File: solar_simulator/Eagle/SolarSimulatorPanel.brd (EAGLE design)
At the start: 150 x 70 mm, 82 parts, among them U1 Blue Driver, U2 Red Driver, U3 Green Driver, X1 MKDSN1,5/2-5,08

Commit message: added manufacturer informaton for temp sensors on solar sim, tweaks to 1u_panel, added very in progress driver for solar simulator.  Documentation inboud
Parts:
- R2, R3, R6: value 137 m -> 250 m
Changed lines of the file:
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@@
 <?xml version="1.0" encoding="utf-8"?>
 <!DOCTYPE eagle SYSTEM "eagle.dtd">
-<eagle version="9.3.0">
+<eagle version="9.4.0">
 <drawing>
 <settings>
@@
 <attribute name="VALUE" x="8.725" y="26.6" size="1.016" layer="27" rot="R270"/>
 </element>
-<element name="R6" library="rcl" library_urn="urn:adsk.eagle:library:334" package="R2010" package3d_urn="urn:adsk.eagle:package:23551/2" value="137 m" x="22.8" y="64.9" smashed="yes">
+<element name="R6" library="rcl" library_urn="urn:adsk.eagle:library:334" package="R2010" package3d_urn="urn:adsk.eagle:package:23551/2" value="250 m" x="22.8" y="64.9" smashed="yes">
 <attribute name="NAME" x="22.025" y="67.005" size="0.7" layer="25" font="vector" ratio="20"/>
 <attribute name="SPICEPREFIX" value="R" x="22.8" y="64.9" size="1.778" layer="27" display="off"/>
 <attribute name="VALUE" x="19.625" y="61.725" size="1.27" layer="27"/>
 </element>
-<element name="R2" library="rcl" library_urn="urn:adsk.eagle:library:334" package="R2010" package3d_urn="urn:adsk.eagle:package:23551/2" value="137 m" x="22.7" y="48.9" smashed="yes">
+<element name="R2" library="rcl" library_urn="urn:adsk.eagle:library:334" package="R2010" package3d_urn="urn:adsk.eagle:package:23551/2" value="250 m" x="22.7" y="48.9" smashed="yes">
 <attribute name="NAME" x="22.225" y="50.605" size="0.7" layer="25" font="vector" ratio="20"/>
 <attribute name="SPICEPREFIX" value="R" x="22.7" y="48.9" size="1.778" layer="27" display="off"/>
 <attribute name="VALUE" x="19.525" y="45.725" size="1.27" layer="27"/>
 </element>
-<element name="R3" library="rcl" library_urn="urn:adsk.eagle:library:334" package="R2010" package3d_urn="urn:adsk.eagle:package:23551/2" value="137 m" x="22.7" y="33.2" smashed="yes">
+<element name="R3" library="rcl" library_urn="urn:adsk.eagle:library:334" package="R2010" package3d_urn="urn:adsk.eagle:package:23551/2" value="250 m" x="22.7" y="33.2" smashed="yes">
 <attribute name="NAME" x="22.325" y="35.005" size="0.7" layer="25" font="vector" ratio="20"/>
 <attribute name="SPICEPREFIX" value="R" x="22.7" y="33.2" size="1.778" layer="27" display="off"/>

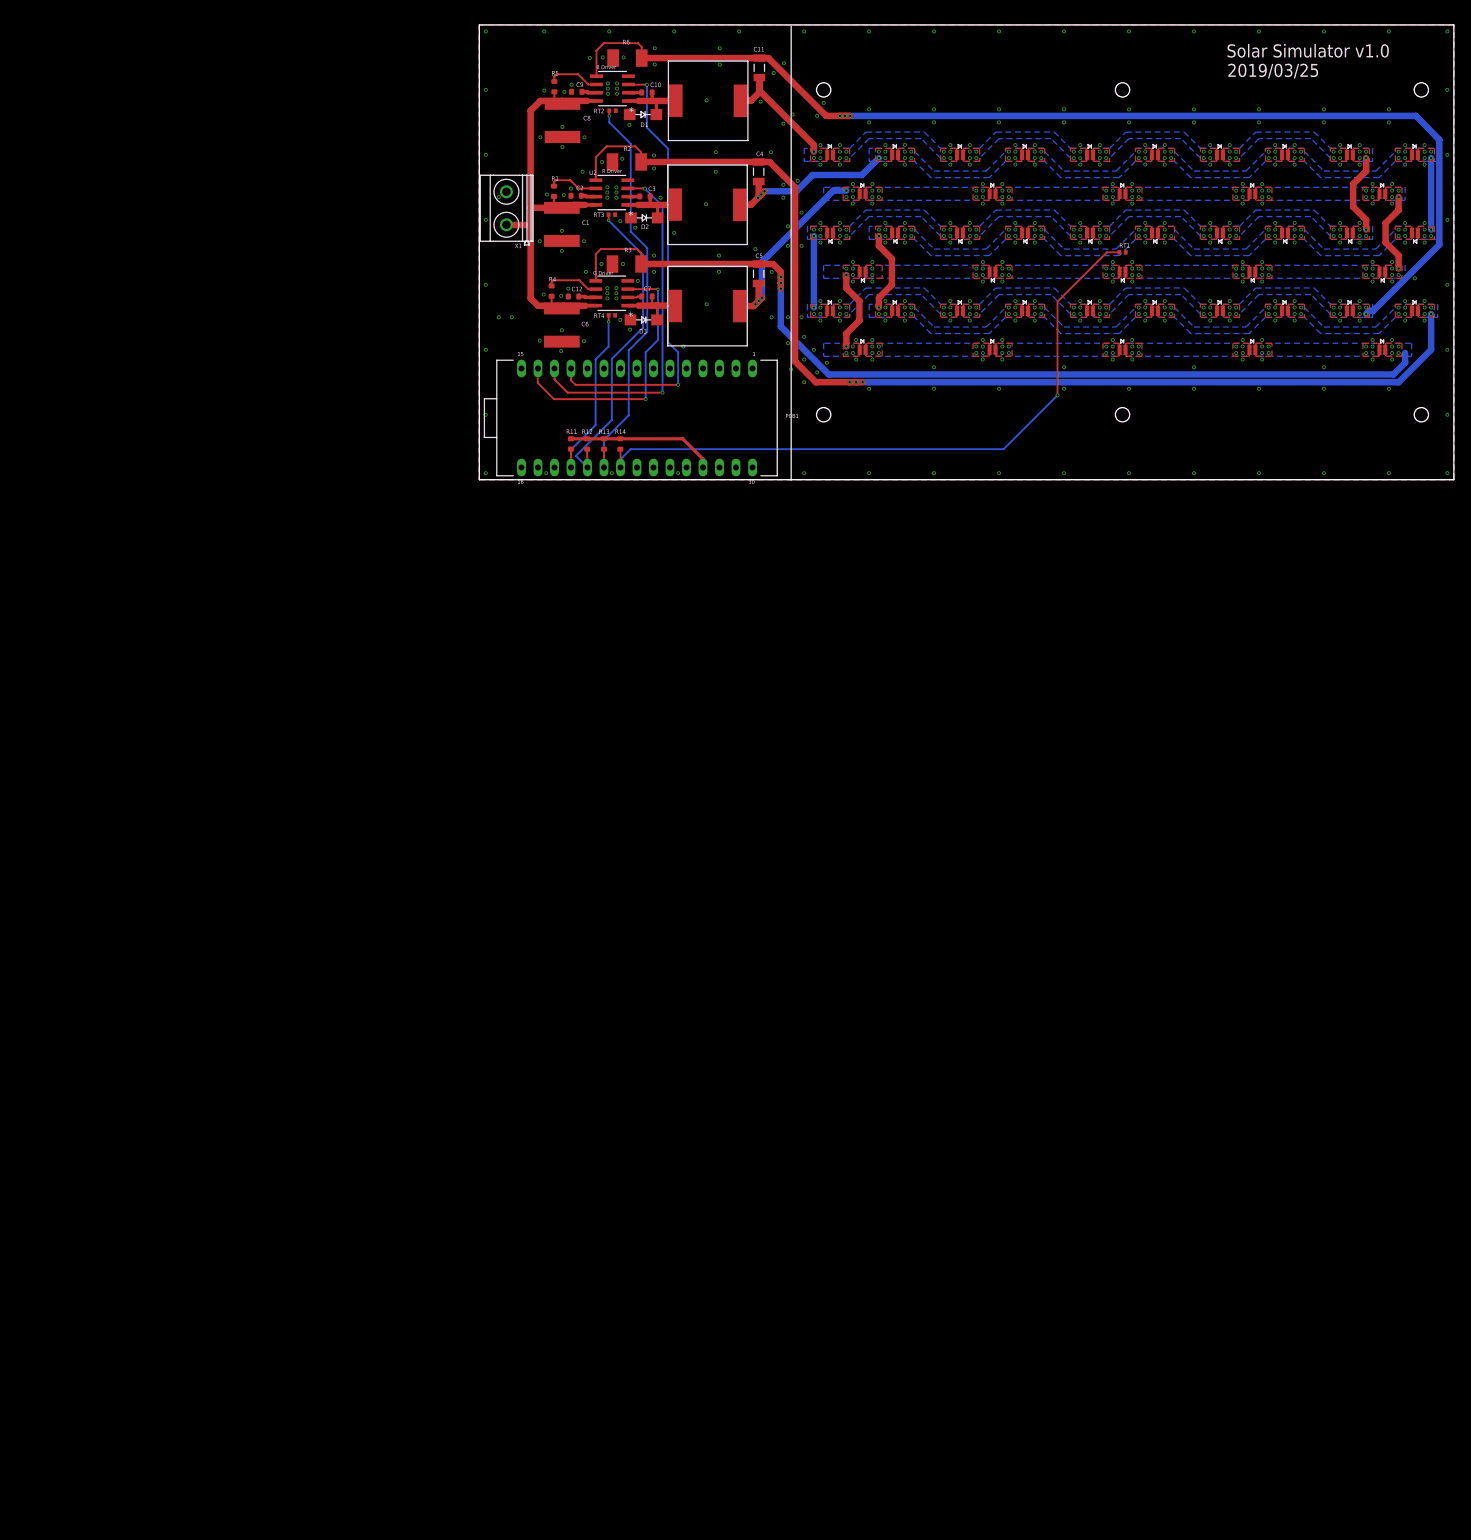
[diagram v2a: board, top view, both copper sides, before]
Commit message: schematic for solar sim 2.0
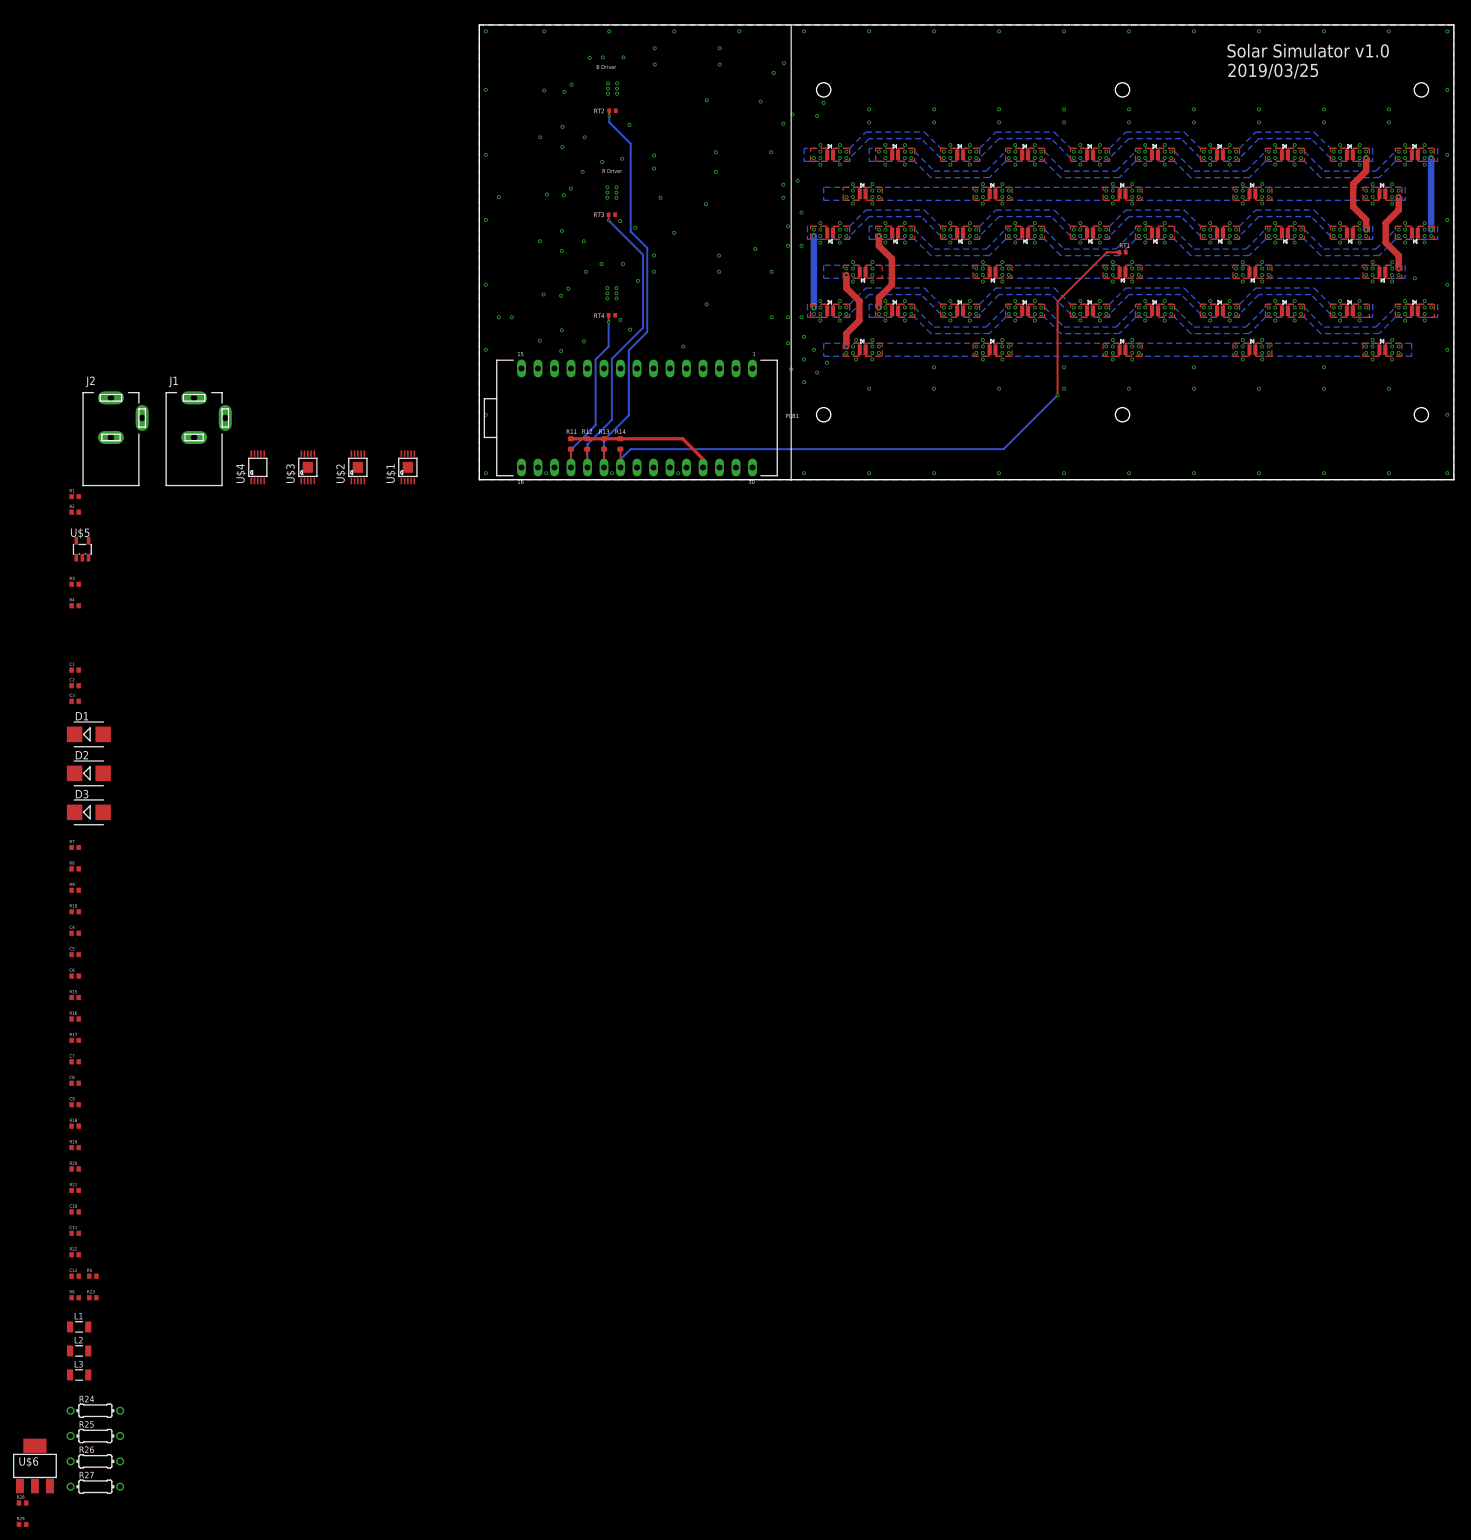
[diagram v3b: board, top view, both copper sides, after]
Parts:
- removed U1: Blue Driver, solarsim:M08A
- removed U2: Red Driver, solarsim:M08A
- removed U3: Green Driver, solarsim:M08A
- removed X1: MKDSN1,5/2-5,08, con-phoenix-508:MKDSN1,5/2-5,08
- added J1, J2: DCJ0202, con-jack:DCJ0202
- added R10, R15, R16, R17, R18, R19, R20, R21, R22, R23, R7, R8, R9: TBD, oresat-rcl:.0402-A-NOSILK
- added R24, R25, R26, R27: (no value), oresat-rcl:0204/7
- added R28: 220, oresat-rcl:.0402-A-NOSILK
- added R29: 10k, oresat-rcl:.0402-A-NOSILK
- added U$1, U$2, U$3: TPS92512, U-TI-TPS92512-buck:MSOP10
- added U$4: MCP4728, U-Microchip-MCP4728-QuadDAC:MSOP10
- added U$5: AP2127, U-Diodes-AP2127-LDO:SOT23-5
- added U$6: NCH-SOT223, Q-MOSFET-NCH-SOT223:SOT223
- C1: value 1 uF 120V -> .1 u; device rcl:C2220K -> oresat-rcl:.0402-A-NOSILK
- C10, C7: value 10nF 25V -> TBD; device oresat-rcl:.0603-B-NOSILK -> oresat-rcl:.0402-A-NOSILK
- C11: value 10uF -> TBD; device oresat-rcl:1206-B -> oresat-rcl:.0402-A-NOSILK
- C12, C9: value 100nF 25V -> TBD; device oresat-rcl:.0603-B-NOSILK -> oresat-rcl:.0402-A-NOSILK
- C2: value 100n 25V -> .1u; device oresat-rcl:.0603-B-NOSILK -> oresat-rcl:.0402-A-NOSILK
- C3: value 10nF 25V -> .1u; device oresat-rcl:.0603-B-NOSILK -> oresat-rcl:.0402-A-NOSILK
- C4, C5: value 10uF -> .1u; device oresat-rcl:1206-B -> oresat-rcl:.0402-A-NOSILK
- C6: value 1 uF 120V -> .1u; device rcl:C2220K -> oresat-rcl:.0402-A-NOSILK
- C8: value 1 uF 120V -> TBD; device rcl:C2220K -> oresat-rcl:.0402-A-NOSILK
- D1, D2, D3: value GF1 -> TBD; device diode:SMA-DO214AC -> diode:SMB
- L1, L2, L3: value 220 uH -> TBD; device solarsim:P1170 -> oresat-rcl:1206-C
- R1: value 597k -> 10k; device oresat-rcl:.0603-B-NOSILK -> oresat-rcl:.0402-A-NOSILK
- R2, R3: value 250 m -> 10k; device rcl:R2010 -> oresat-rcl:.0402-A-NOSILK
- R4: value 597k -> 100k; device oresat-rcl:.0603-B-NOSILK -> oresat-rcl:.0402-A-NOSILK
- R5: value 597k -> TBD; device oresat-rcl:.0603-B-NOSILK -> oresat-rcl:.0402-A-NOSILK
- R6: value 250 m -> TBD; device rcl:R2010 -> oresat-rcl:.0402-A-NOSILK
- moved R6 208.9 mm to (-62.2, -125.9)
- moved C11 208.0 mm to (-62.2, -116.0), turned to 0 degrees
- moved L1 203.9 mm to (-61.6, -130.4)
- moved R5 196.4 mm to (-59.5, -122.6), turned to 0 degrees
- moved C10 193.5 mm to (-62.2, -112.7)
- moved L2 192.9 mm to (-61.6, -134.1)
- moved L3 182.5 mm to (-61.6, -137.8)
- moved C9 174.0 mm to (-62.2, -96.2), turned to 0 degrees
- moved C12 169.2 mm to (-62.2, -122.6), turned to 0 degrees
- moved C8 166.1 mm to (-62.2, -92.9), turned to 0 degrees
- moved C4 157.5 mm to (-62.2, -69.8), turned to 0 degrees
- moved C5 148.5 mm to (-62.2, -73.1), turned to 0 degrees
- moved C7 147.0 mm to (-62.2, -89.6)
- moved D1 128.0 mm to (-60.1, -39.2)
- moved C6 125.1 mm to (-62.2, -76.4), turned to 0 degrees
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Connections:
- removed net 3V3: PCB1.17
- removed net BLUE-OUT: BLUE1.ANODE, C11.1, L1.P$2
- removed net BLUE-RTN: BLUE15.CATHODE, C11.2, R6.2, U1.5
- removed net D10/PWM_R: PCB1.13, U2.3
- removed net D11/PWM_G: PCB1.14, U3.3
- removed net D9/PWM_B: PCB1.12, U1.3
- removed net GREEN-RTN: C5.2, GREEN15.CATHODE, R3.2, U3.5
- removed net GRN-OUT: C5.1, GREEN1.ANODE, L3.P$2
- removed net RED-OUT: C4.1, L2.P$2, RED1.ANODE
- removed net RED-RTN: C4.2, R2.2, RED15.CATHODE, U2.5
- removed net VPP: C1.1, C6.1, C8.1, R1.2, R4.2, R5.2, U1.8, U2.8, U3.8, X1.1
- new net +12: J1.3
- new net +3V3: PCB1.17, U$5.1
- new net +56V: J2.3
- new net N$24: C2.2, D2.C, L2.1, U$2.10
- new net N$28: PCB1.14, R4.1, U$4.5
- new net N$3: PCB1.24, R1.1, U$4.2
- new net N$47: C1.1, U$3.1
- new net N$51: C2.1, U$2.1
- new net N$54: R16.2, U$2.7
- new net N$55: R17.2, U$3.7
- new net N$58: R15.2, U$1.7
- new net N$59: C8.2, R16.1, R19.2, RED15.CATHODE
- new net N$60: C8.1
- new net N$61: C9.2, GREEN15.CATHODE, R17.1, R20.2
- new net N$62: C9.1
- new net N$63: R21.2, U$2.5
- new net N$64: U$1.6, U$4.8
- new net N$65: R22.2, U$1.5
- new net N$66: C10.1, U$2.8
- new net N$67: C11.1, U$1.8
- new net N$68: U$3.6, U$4.6
- new net N$69: GREEN1.ANODE, L1.2
- new net N$70: L2.2, RED1.ANODE
- new net N$71: BLUE15.CATHODE, C7.2, R15.1, R18.2
- new net N$72: BLUE1.ANODE, L3.2
- new net N$73: R24.1, U$6.3
- new net N$74: R24.2, R25.1
- new net N$75: R25.2, R26.1
- new net N$76: R26.2, R27.1
- new net N$78: R28.1, R29.2, U$6.1
- new net N$79: PCB1.16, R28.2
- new net VCC: U$6.2, U$6.4
- new net VCC/2: C4.1, C5.1, R6.2, R8.2, U$2.2, U$3.2
- new net VCC/3: C6.1, R10.2, U$1.2
- net +5V: now also R1.2, R2.2, R3.2
- net GND: now also C10.2, C11.2, C4.2, C5.2, J1.1, J2.1, R18.1, R19.1, R20.1, R21.1, R22.1, R23.1, R27.2, R29.1, R5.1, R7.1, R9.1, U$1.9, U$1.GND, U$2.9, U$2.GND, U$3.9, U$3.GND, U$4.10, U$5.2; no longer C1.2, C2.2, C8.2, C9.2, R2.1, R3.1, R6.1, U1.4, U2.4, U3.4, X1.2
- net N$1: now also PCB1.23, R2.1, U$4.3; no longer C7.2, D3.K, L3.P$1, U3.1
- net N$18: now also U$2.6, U$4.7; no longer R5.1, U1.6
- net N$19: now also R23.2, U$3.5; no longer R4.1, U3.6
- net N$22: now also C3.2, C7.1, D3.C, L3.1, U$1.10; no longer C3.1, U2.2
- net N$25: now also C1.2, D1.C, L1.1, U$3.10; no longer C3.2, D2.K, L2.P$1, U2.1
- net N$32: now also PCB1.15, R3.1, U$4.4; no longer C7.1, U3.2
- net N$33: now also U$3.8; no longer U3.7
- net N$34: now also C3.1, U$1.1; no longer C10.2, D1.K, L1.P$1, U1.1
- net N$4: now also R4.2, U$4.1, U$5.5; no longer C2.1, U2.7
- net N$52: now also R7.2, R8.1, U$2.3; no longer C10.1, U1.2
- net N$53: now also R10.1, R9.2, U$1.3; no longer C9.1, U1.7
- net N$6: now also R5.2, R6.1, U$3.3; no longer R1.1, U2.6
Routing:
- net BLUE-RTN: track 174.8 -> 0.00 mm, vias 7 -> 3
- net RED-RTN: track 174.0 -> 0.00 mm, vias 7 -> 3
- net GREEN-RTN: track 147.0 -> 0.00 mm, vias 7 -> 4
- net VPP: track 69.8 -> 0.00 mm
- net D9/PWM_B: track 69.6 -> 0.00 mm, vias 2 -> 0
- net D10/PWM_R: track 54.3 -> 0.00 mm, vias 2 -> 0
- net D11/PWM_G: track 42.2 -> 0.00 mm, vias 2 -> 0
- net GRN-OUT: track 31.1 -> 0.00 mm, vias 7 -> 3
- net RED-OUT: track 28.2 -> 0.00 mm, vias 7 -> 3
- net BLUE-OUT: track 20.6 -> 0.00 mm, vias 4 -> 3
- net N$1: track 10.9 -> 0.00 mm
- net N$34: track 10.7 -> 0.00 mm
- net N$25: track 10.6 -> 0.00 mm
- net N$19: track 8.09 -> 0.00 mm
- net N$18: track 8.03 -> 0.00 mm
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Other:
- board text removed: "G Driver"

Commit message: forgot a pullup
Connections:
- new net N$80: U$5.1, U$5.3
- net +3V3: no longer U$5.1
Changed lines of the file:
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@@
 <signal name="+3V3">
 <contactref element="PCB1" pad="17"/>
-<contactref element="U$5" pad="1"/>
-<wire x1="9.03" y1="1.88" x2="-62.05" y2="-12" width="0" layer="19" extent="1-1"/>
 </signal>
 <signal name="N$4">
@@
 <wire x1="-70.7114" y1="-154.8988" x2="-70.85" y2="-157.5" width="0" layer="19" extent="1-1"/>
 </signal>
+<signal name="N$80">
+<contactref element="U$5" pad="1"/>
+<contactref element="U$5" pad="3"/>
+<wire x1="-60.15" y1="-12" x2="-62.05" y2="-12" width="0" layer="19" extent="1-1"/>
+</signal>
 </signals>
